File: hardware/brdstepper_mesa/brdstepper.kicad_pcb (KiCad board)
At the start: 4 copper layers, 28 x 28 mm, 87 parts, among them J3 MOTOR, J4 SMART-SERIAL, U1 STM32G473CEU6, U2 DRV8876RGTR, U3 DRV8876RGTR, U4 AS5047P-ATSM, U5 TLV75533PDBVR, U6 TPS560430XDBVR, U8 SN65HVD30DR, Y1 8MHz

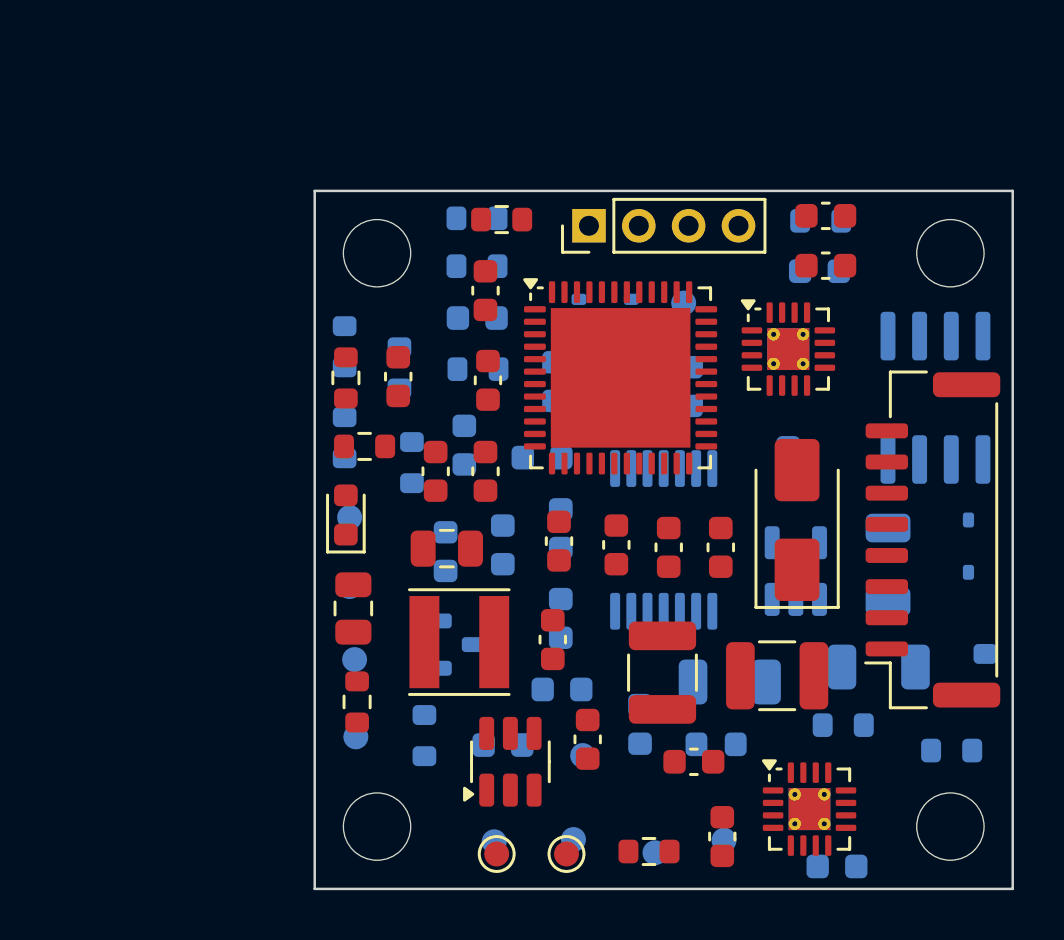
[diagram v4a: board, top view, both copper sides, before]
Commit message: brdstepper: routed snapshot with GND plane fanout, partial (WIP)
First plane-aware BrdRoute runs (150 s cap): serial 70/129 connections,
CAN 69/135, not complete, DRC not clean. Longer runs are in progress.

Co-Authored-By: Claude Sonnet 5.5 <noreply@anthropic.com>
Claude-Session: https://claude.ai/code/session_017CSpK2B8oMBAmr39Kq1RSC
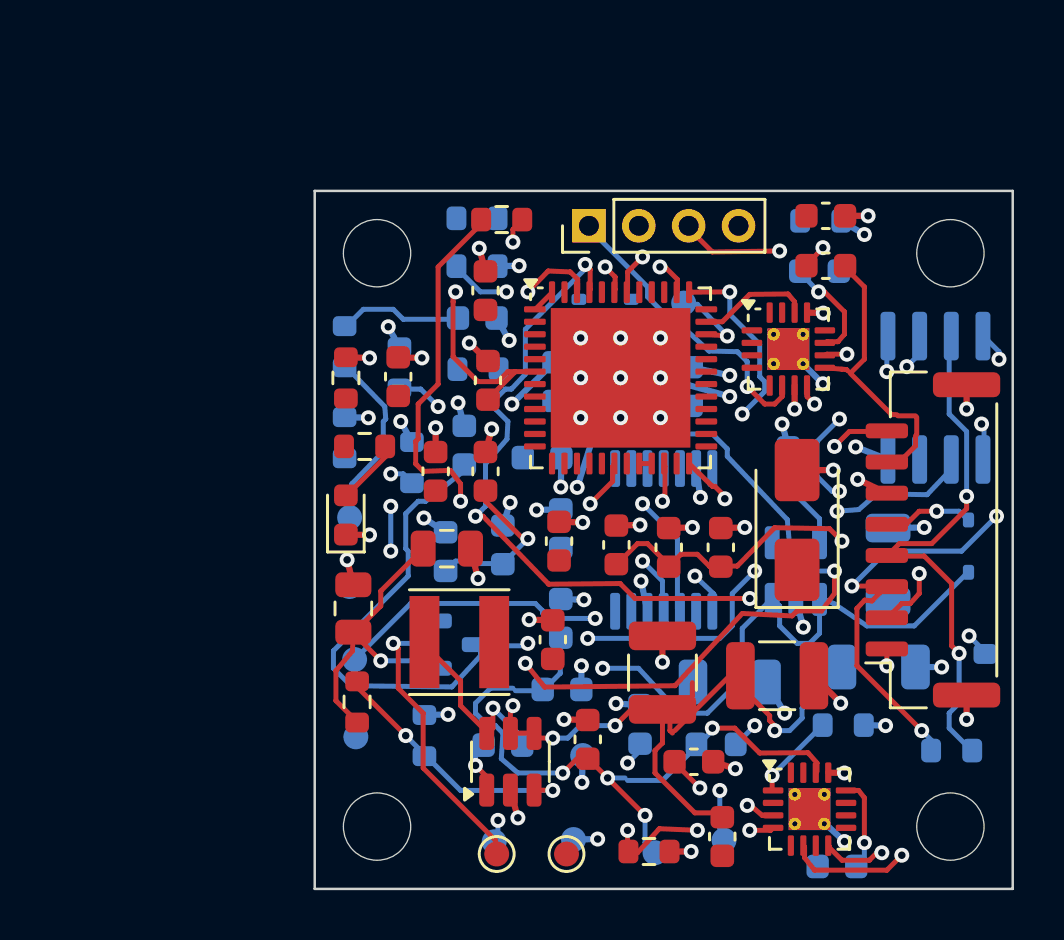
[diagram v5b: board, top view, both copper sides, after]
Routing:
- net GND: track 0.00 -> 71.0 mm, vias 0 -> 69
- net VM: track 0.00 -> 60.0 mm, vias 0 -> 7
- net OSC_OUT: track 0.00 -> 53.8 mm, vias 0 -> 3
- net 5V: track 0.00 -> 46.3 mm, vias 0 -> 2
- net 3V3: track 0.00 -> 45.1 mm, vias 0 -> 6
- net COIL_B+: track 0.00 -> 39.5 mm, vias 0 -> 2
- net EN_RAW: track 0.00 -> 39.0 mm, vias 0 -> 4
- net SS_RX: track 0.00 -> 36.6 mm, vias 0 -> 4
- net COIL_B-: track 0.00 -> 32.1 mm, vias 0 -> 3
- net SWCLK: track 0.00 -> 25.0 mm, vias 0 -> 3
- net SS_RX+: track 0.00 -> 24.4 mm, vias 0 -> 4
- net SS_RX-: track 0.00 -> 21.7 mm, vias 0 -> 2
- net VDDA: track 0.00 -> 21.5 mm, vias 0 -> 2
- net TP_PB11: track 0.00 -> 19.7 mm, vias 0 -> 2
- net TP_PB10: track 0.00 -> 19.0 mm, vias 0 -> 2
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
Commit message: brdstepper: routed with 0.127 mm rules, plane fanout; ~75% complete (WIP)
Both boards routed with BrdRoute (900 s cap): serial 100/129 connections
(77.5%), CAN 100/135 (74.1%). Not complete, DRC not clean (KiCad: serial
11 clearance, 2 edge, 29 unconnected; CAN 14, 2, 35).

kigen route fixes found on the way:
- load_bare did not strip old copper (indentation): routes piled up
- the temp-dir board lost the project's design rules and net classes
  (router saw 0.2 mm clearance): project copied in, rules written back
- default board via (0.6 mm) offered next to the net class via: first only
- net classes 0.127 mm clearance, 0.15 / 0.3 mm tracks, 0.5 / 0.25 mm vias

BOM and renders regenerated.

Co-Authored-By: Claude Sonnet 5.5 <noreply@anthropic.com>
Claude-Session: https://claude.ai/code/session_017CSpK2B8oMBAmr39Kq1RSC
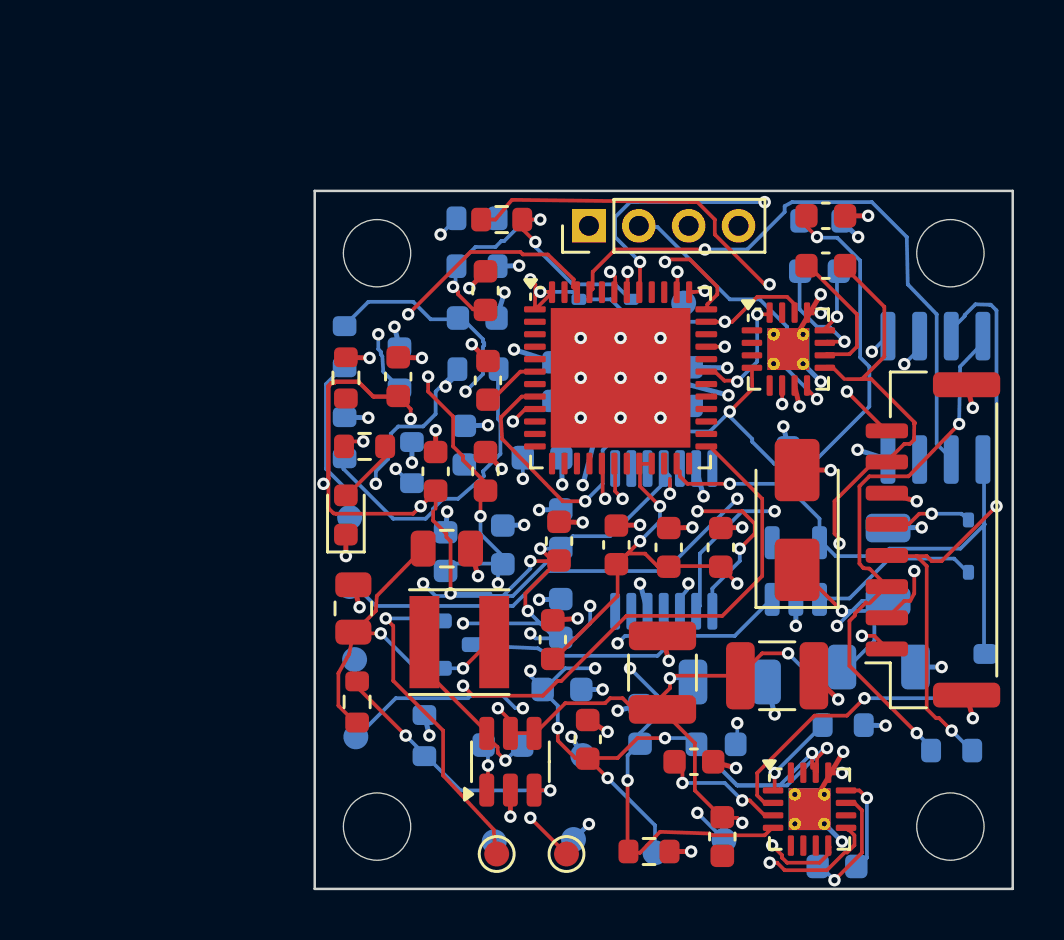
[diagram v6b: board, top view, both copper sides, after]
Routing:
- net 3V3: track 45.1 -> 151.0 mm, vias 6 -> 25
- net OSC_OUT: track 53.8 -> 2.35 mm, vias 3 -> 0
- net COIL_B+: track 39.5 -> 0.00 mm, vias 2 -> 0
- net SWDIO: track 0.00 -> 35.0 mm, vias 0 -> 2
- net IPROPI_A: track 0.33 -> 34.2 mm, vias 0 -> 3
- net LED: track 0.00 -> 32.7 mm, vias 0 -> 2
- net ENC_CLK: track 0.00 -> 31.1 mm, vias 0 -> 3
- net USB_DM: track 0.00 -> 25.2 mm, vias 0 -> 2
- net 5V: track 46.3 -> 22.6 mm, vias 2 -> 0
- net VM: track 60.0 -> 82.3 mm, vias 7 -> 12
- net TP_PB11: track 19.7 -> 0.00 mm, vias 2 -> 0
- net TP_PB10: track 19.0 -> 0.00 mm, vias 2 -> 0
- net EN_RAW: track 39.0 -> 21.5 mm, vias 4 -> 2
- net NRST: track 0.00 -> 17.0 mm, vias 0 -> 2
- net IPROPI_B: track 10.8 -> 27.6 mm, vias 4 -> 3
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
